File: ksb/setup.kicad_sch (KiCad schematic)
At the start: 35 parts, among them U4 X850744-001, Y1 Crystal_GND24

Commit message: Internal Connectors
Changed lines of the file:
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@@
-		)
-	)
-	(bus
-		(pts
-			(xy 102.87 127) (xy 107.95 127)
-		)
-		(stroke
-			(width 0)
-			(type default)
 		)
 	)
@@
 	(hierarchical_label "SMB{I2C}"
 		(shape bidirectional)
-		(at 107.95 127 0)
+		(at 102.87 127 270)
 		(effects
 			(font
 				(size 1.27 1.27)
 			)
-			(justify left)
-		)
-	)
+			(justify right)
+		)
+	)

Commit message: Cleanup & Debug I/O
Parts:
- removed TP12: TestPoint, symbol Connector:TestPoint
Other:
- moved on the sheet: TP13, TP15, TP16

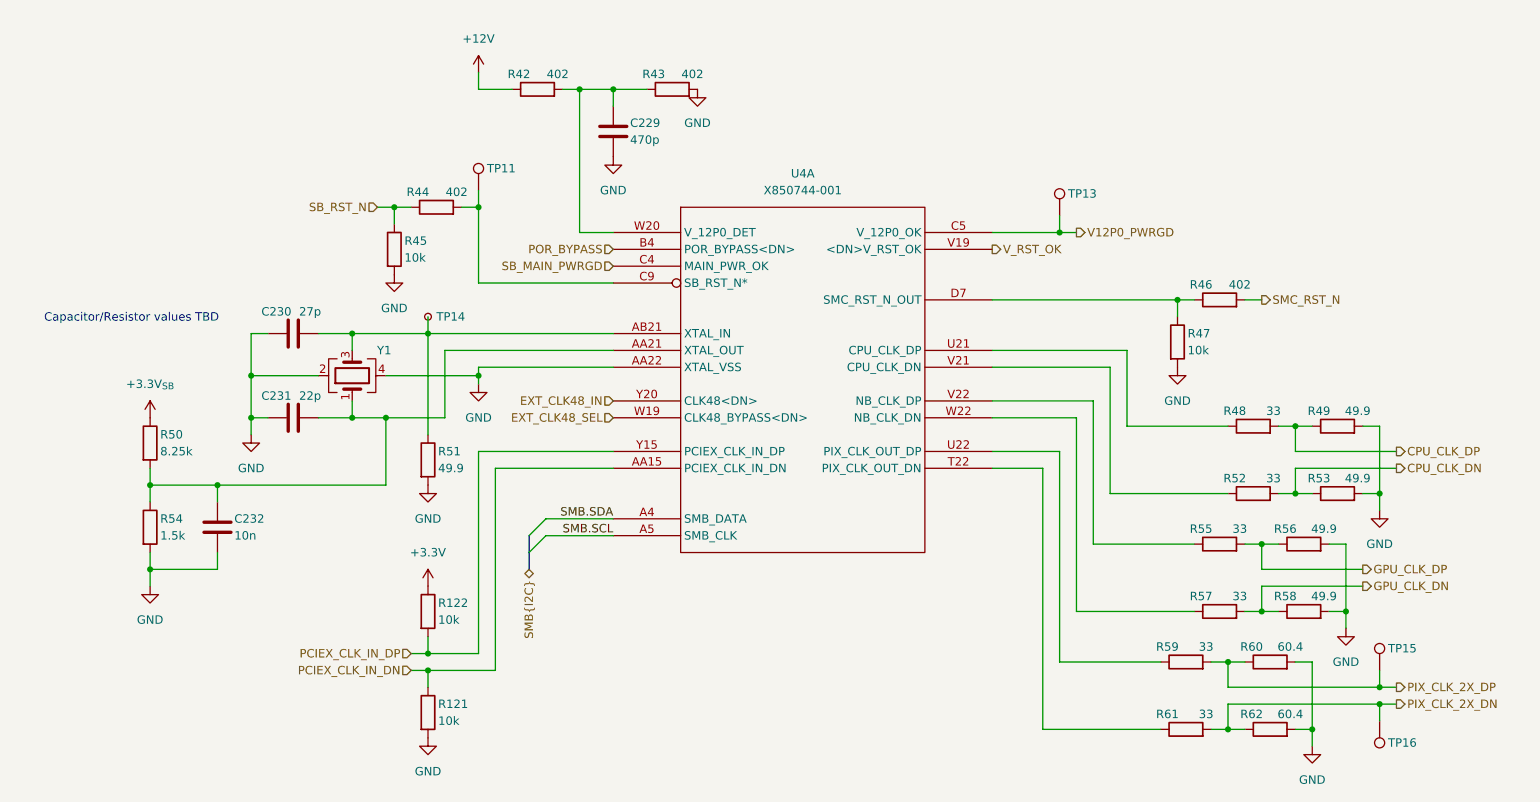
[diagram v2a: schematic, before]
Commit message: Nand Flash, Sata Connectors and removing (hopefully) unnecessary things
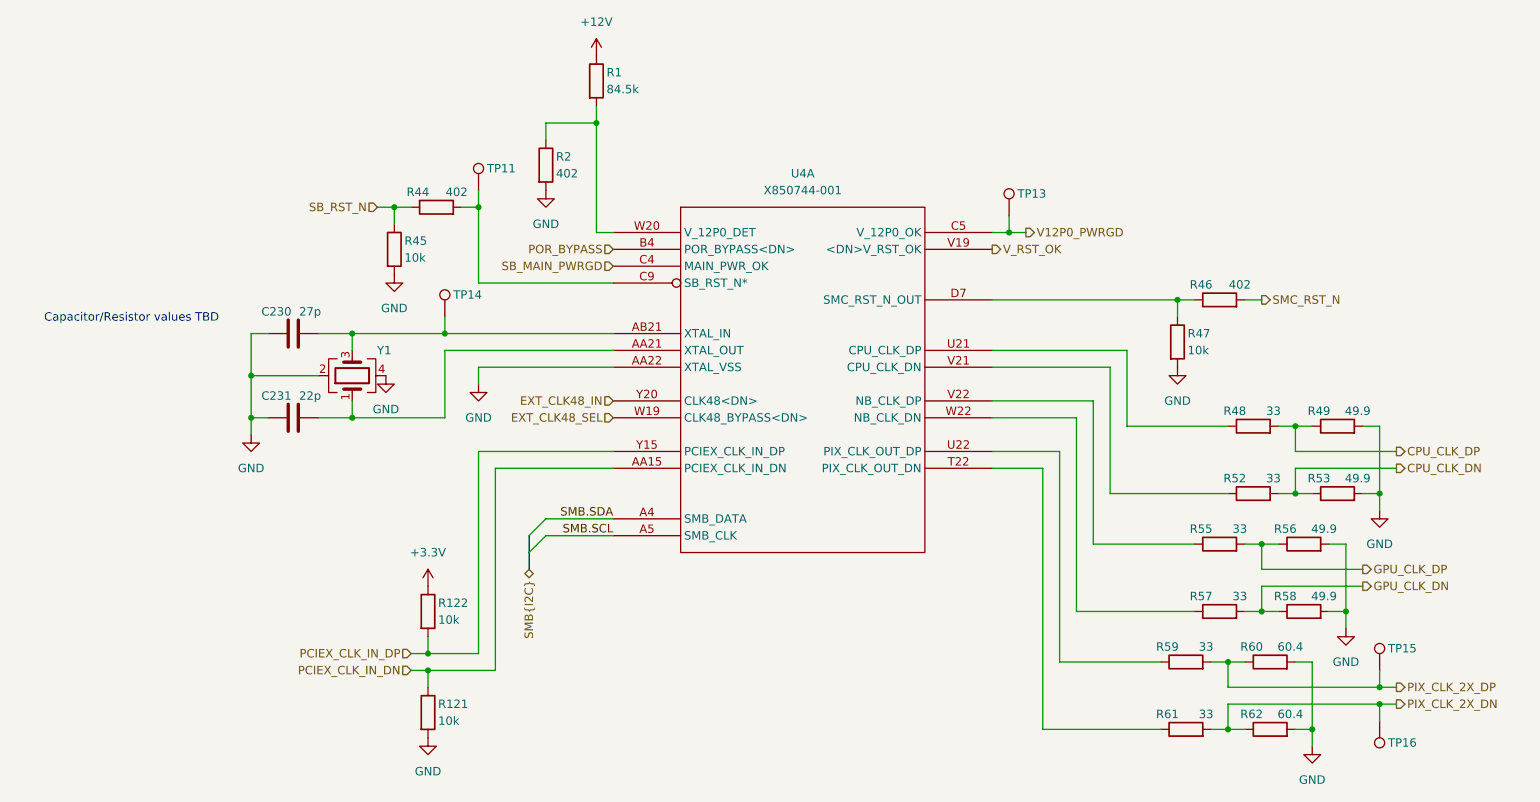
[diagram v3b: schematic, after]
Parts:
- removed C229: 470p, symbol Device:C
- removed C232: 10n, symbol Device:C
- removed R42, R43: 402, symbol Device:R
- removed R50: 8.25k, symbol Device:R
- removed R51: 49.9, symbol Device:R
- removed R54: 1.5k, symbol Device:R
- removed TP14: TestPoint_Small, symbol Connector:TestPoint_Small
- added R1: 84.5k, symbol Device:R
- added R2: 402, symbol Device:R
- added TP14: TestPoint, symbol Connector:TestPoint
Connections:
- net +12V: now also R1.1
- net GND: now also R2.2
- net at C230.2, U4.AB21 (XTAL_IN), Y1.3: now also TP14.1
- net at U4.W20 (V_12P0_DET): now also R1.2, R2.1
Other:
- moved on the sheet: TP13

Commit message: Multipurpose and standby power rails, Reannotated schematic
Added V_1P2, V_1P8, V_5P0DUAL, V_EFUSE, V_GPUPCIE, V_3P3STBY and V_1P2STBY
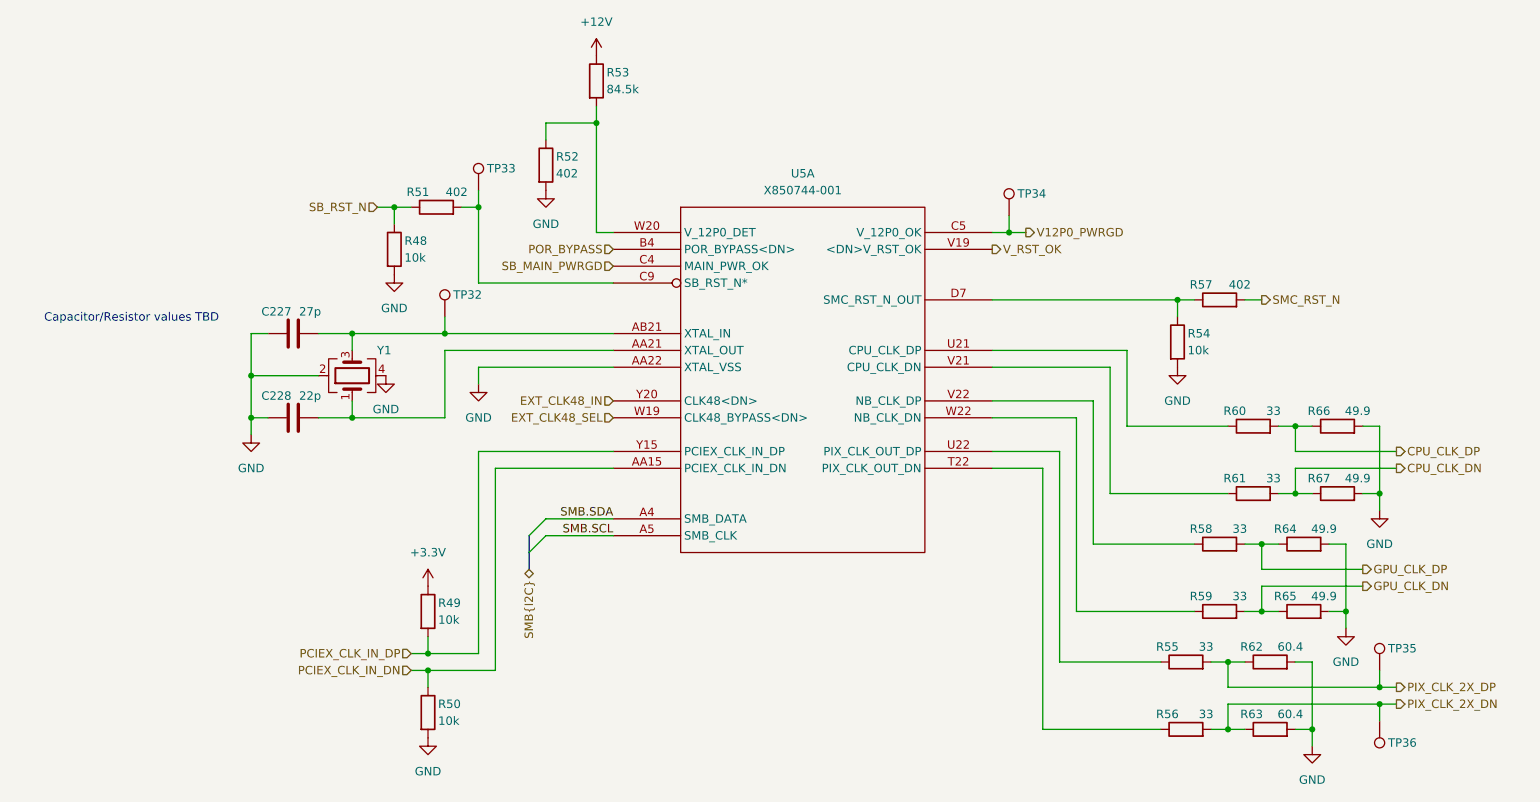
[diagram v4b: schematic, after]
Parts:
- renumbered C230 to C227, C231 to C228, R45 to R48, R122 to R49, R121 to R50, R44 to R51, R2 to R52, R1 to R53, R47 to R54, R59 to R55, R61 to R56, R46 to R57, R55 to R58, R57 to R59, R48 to R60, R52 to R61, R60 to R62, R62 to R63, R56 to R64, R58 to R65, R49 to R66, R53 to R67, TP14 to TP32, TP11 to TP33, TP13 to TP34, TP15 to TP35, TP16 to TP36, U4 to U5
